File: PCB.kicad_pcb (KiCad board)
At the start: 2 copper layers, 60 x 60 mm, 53 parts, among them J1 USB_C_Receptacle_USB2.0_16P, J10 Conn_01x05_Pin, J11 Conn_01x05_Pin, J12 Conn_01x03_Pin, J2 Conn_01x04_Pin, J3 Conn_01x04_Pin, J4 Conn_01x07_Pin, J5 Conn_01x02_Pin, J6 Conn_01x02_Pin, J7 Conn_01x02_Pin, J8 Conn_01x04_Pin, J9 Conn_01x07_Pin, SW1 SW_Push, SW2 SW_Push, U1 TMC2209_SILENTSTEPSTICK, U2 TMC2209_SILENTSTEPSTICK, U3 D3V3XA4B10LP, U4 AMS1117-3.3 (UMW), U5 TMC2209_SILENTSTEPSTICK, U6 ESP32-S3-WROOM-1

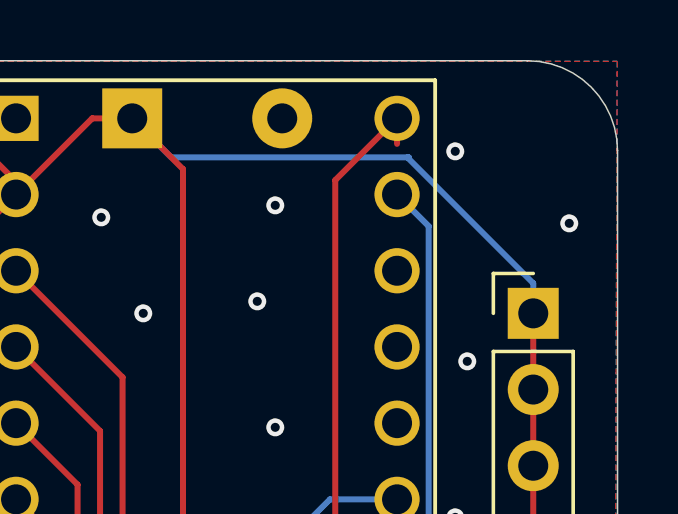
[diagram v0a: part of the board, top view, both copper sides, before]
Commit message: ajout trous de montage
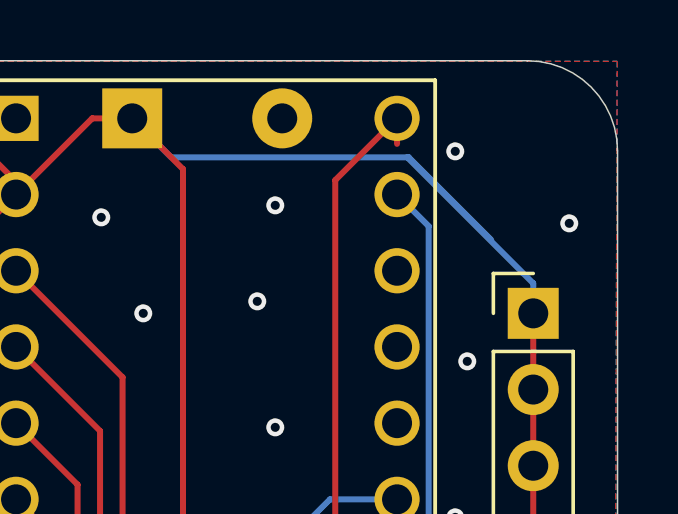
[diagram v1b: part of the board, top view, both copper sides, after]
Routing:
- net VCC_5V: track 326.4 -> 330.3 mm
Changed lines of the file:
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@@
+	(segment
+		(start 163.25 76.2)
+		(end 166 78.95)
+		(width 0.2)
+		(layer "B.Cu")
+		(net 4)
+	)
 	(segment
 		(start 163.25 76.2)

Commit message: BOM à réaliser
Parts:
- added H1: MountingHole, MountingHole:MountingHole_3.2mm_M3, F.Cu at (113.2, 76.0)
- added H2: MountingHole, MountingHole:MountingHole_3.2mm_M3, F.Cu at (167.2, 76.0)
- added H3: MountingHole, MountingHole:MountingHole_3.2mm_M3, F.Cu at (113.2, 130.0)
- added H4: MountingHole, MountingHole:MountingHole_3.2mm_M3, F.Cu at (167.2, 130.0)

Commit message: Test DRC OK
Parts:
- C1, C10, C2, C4, C9: footprint Resistor_SMD:R_01005_0402Metric -> Capacitor_SMD:C_0805_2012Metric_Pad1.18x1.45mm_HandSolder
- C5, C7: footprint Resistor_SMD:R_0603_1608Metric -> Capacitor_SMD:C_1206_3216Metric_Pad1.33x1.80mm_HandSolder
- R1: footprint Resistor_SMD:R_01005_0402Metric -> Resistor_SMD:R_1206_3216Metric_Pad1.30x1.75mm_HandSolder
- R2, R3, R4, R5: footprint Resistor_SMD:R_01005_0402Metric -> Resistor_SMD:R_0805_2012Metric_Pad1.20x1.40mm_HandSolder
- moved R1 12.9 mm to (162.6, 130.8), turned to 0 degrees
- moved C9 7.94 mm to (158.8, 130.0)
- moved C10 6.78 mm to (156.6, 130.0)
- moved R3 5.54 mm to (154.8, 123.2), turned to -90 degrees
- moved C4 5.32 mm to (160.6, 111.8)
- moved C2 2.01 mm to (154.4, 130.0)
- moved SW2 1.91 mm to (151.4, 129.9)
- moved R2 1.88 mm to (159.2, 114.8), turned to 90 degrees
- moved J6 1.81 mm to (164.8, 126.1)
- moved D1 1.74 mm to (159.4, 126.2)
- moved D2 1.69 mm to (157.6, 126.2)
- moved JP3 1.58 mm to (140.2, 92.5)
- moved JP4 1.58 mm to (140.2, 90.0)
- moved C5 1.53 mm to (166.6, 111.4), turned to 0 degrees
- moved SW1 1.26 mm to (125.2, 129.9)
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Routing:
- net VCC_5V: track 330.3 -> 540.8 mm, vias 4 -> 7
- net GND: track 24.4 -> 183.7 mm, vias 82 -> 112
- net MOTORA2: track 18.0 -> 53.4 mm
- net MOTORA1: track 21.6 -> 43.2 mm
- net MOTORB1: track 22.3 -> 43.9 mm
- net MOTORC1: track 21.3 -> 42.6 mm
- net MOTORC2: track 17.7 -> 35.4 mm
- net MOTORB2: track 17.7 -> 35.3 mm
- net MOTORA3: track 14.4 -> 28.8 mm
- net MOTORC3: track 14.1 -> 28.2 mm
- net MOTORB3: track 14.1 -> 28.2 mm
- net MOTORA4: track 11.5 -> 23.4 mm
- net MOTORB4: track 11.2 -> 22.8 mm
- net MOTORC4: track 11.2 -> 22.7 mm
- net ESP32_EN: track 10.1 -> 21.4 mm, vias 0 -> 2
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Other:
- board text added: "I²C"
